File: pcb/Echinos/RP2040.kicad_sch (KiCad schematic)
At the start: 21 parts, among them U2 RP2040, X1 ASE-12MHz

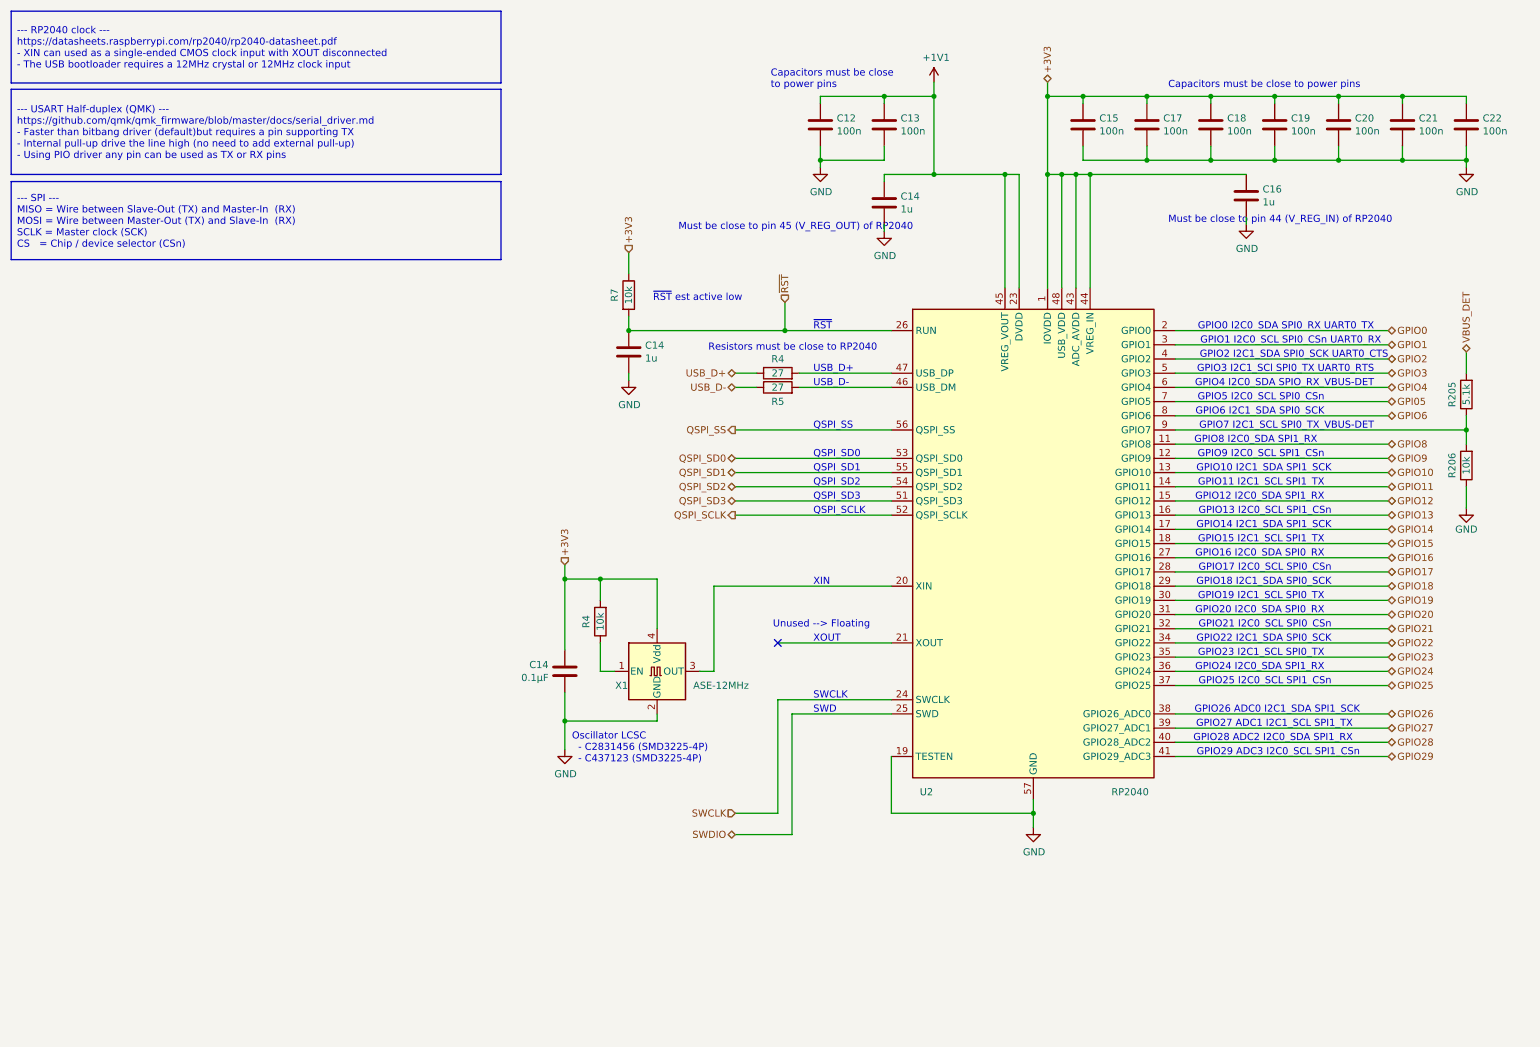
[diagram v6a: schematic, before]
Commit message: ✨ 🚧 [PCB] - Halves are now connected with 5.0V power to be able to expose it to modules (see VIK standard). Update the whole routing to make this happens. VBUS and 5.0V are now split with a schottky diode to still be able to detect when USB is plugged but avoid reverse current in case power comes from the other half. Add ESD events protection to SATA connector.
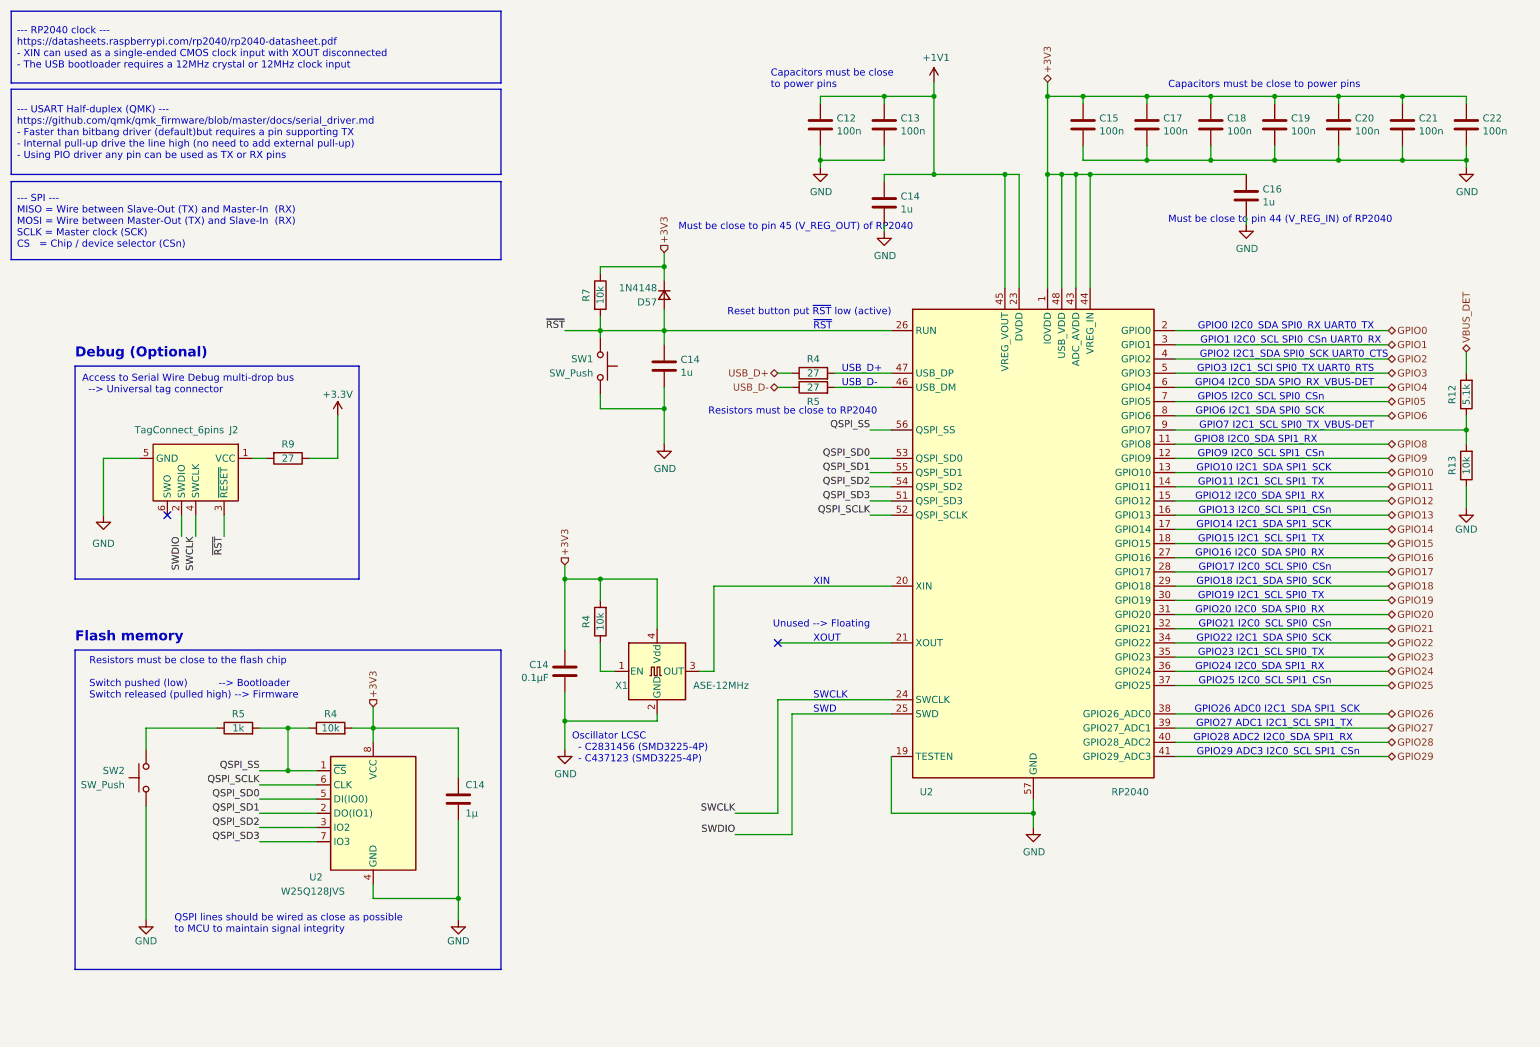
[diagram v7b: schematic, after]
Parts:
- added C14: 1µ, Capacitor_SMD:C_0603_1608Metric_Pad1.08x0.95mm_HandSolder, symbol Device:C
- added D57: 1N4148, Diode_SMD:D_SOD-323_HandSoldering, symbol Device:D_Small
- added J2: TagConnect_6pins, Connector:Tag-Connect_TC2030-IDC-FP_2x03_P1.27mm_Vertical, symbol Connector:Conn_ARM_SWD_TagConnect_TC2030
- added R4: 10k, Resistor_SMD:R_0402_1005Metric_Pad0.72x0.64mm_HandSolder, symbol Device:R
- added R5: 1k, Resistor_SMD:R_0402_1005Metric_Pad0.72x0.64mm_HandSolder, symbol Device:R
- added R9: 27, Resistor_SMD:R_0402_1005Metric_Pad0.72x0.64mm_HandSolder, symbol Device:R
- added SW1, SW2: SW_Push, Button_Switch_SMD:SW_SPST_CK_KXT3, symbol Switch:SW_Push
- added U2: W25Q128JVS, Package_SO:SOIC-8_5.23x5.23mm_P1.27mm, symbol Memory_Flash:W25Q128JVS
- renumbered R205 to R12, R206 to R13
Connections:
- net +3V3: now also C14.1, D57.1 (K), R4.2, U2.8 (VCC)
- net GND: now also C14.2, J2.5 (GND), SW1.2, SW2.1, U2.4 (GND)
- net QSPI_SCLK: now also U2.6 (CLK)
- net QSPI_SD0: now also U2.5 (DI(IO0))
- net QSPI_SD1: now also U2.2 (DO(IO1))
- net QSPI_SD2: now also U2.3 (IO2)
- net QSPI_SD3: now also U2.7 (IO3)
- net QSPI_SS: now also R4.1, R5.2, U2.1 (~{CS})
- net SWCLK: now also J2.4 (SWCLK)
- net SWDIO: now also J2.2 (SWDIO)
- net ~{RST}: now also D57.2 (A), J2.3 (~{RESET}), SW1.1
- new net: R5.1, SW2.2
- new net: J2.1 (VCC), R9.2
- new net +3.3V: R9.1
- no-connect marks 1 -> 2
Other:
- note added: "Access to Serial Wire Debug multi-drop bus --> Universal tag connector"
- note added: "Debug (Optional)"
- note added: "Flash memory"
- note added: "QSPI lines should be wired as close as possible to MCU to maintain signal integrity"
- note added: "Reset button put ~{RST} low (active)"
- note added: "Resistors must be close to the flash chip Switch pushed (low) --> Bootloader Switch released (pulled high) --> Firmware"
- note removed: "QSPI_SCLK"
- note removed: "QSPI_SD0"
- note removed: "QSPI_SD1"
- note removed: "QSPI_SD2"
- note removed: "QSPI_SD3"
- note removed: "QSPI_SS"
- note removed: "~{RST} est active low"
- moved on the sheet: C14, R4, R5, R7

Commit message: ♻️ [PCB] - Now using WSON package for flash memory chip to reduce component height. This allows FPC and memory to be closer freeing pcb space for 6 pins header.
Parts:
- U2: footprint Package_SO:SOIC-8_5.23x5.23mm_P1.27mm -> Package_SON:WSON-8-1EP_6x5mm_P1.27mm_EP3.4x4mm; LCSC C113767 -> C190862
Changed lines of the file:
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@@
       (effects (font (size 1.27 1.27)) (justify left))
     )
-    (property "Footprint" "Package_SO:SOIC-8_5.23x5.23mm_P1.27mm" (at 78.74 156.21 0)
+    (property "Footprint" "Package_SON:WSON-8-1EP_6x5mm_P1.27mm_EP3.4x4mm" (at 78.74 156.21 0)
       (effects (font (size 1.27 1.27)) hide)
     )
@@
       (effects (font (size 1.27 1.27)) hide)
     )
-    (property "LCSC" "C113767" (at 78.74 156.21 0)
+    (property "LCSC" "C190862" (at 78.74 156.21 0)
       (effects (font (size 1.27 1.27)) hide)
     )
